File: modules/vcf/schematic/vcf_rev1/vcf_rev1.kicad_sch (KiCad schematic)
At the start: 0 parts

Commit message: Added project library Added 2N2978
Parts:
- added Q1: 2N2978, ProjectLib_Transient:TO-5-6, symbol ProjectLib_Transient:2N2978
- added Q2: BC548, Package_TO_SOT_THT:TO-92_Inline, symbol Transistor_BJT:BC548
- added R1, R2, R3, R4: 330, Resistor_THT:R_Axial_DIN0207_L6.3mm_D2.5mm_P10.16mm_Horizontal, symbol Device:R_US
- added RV1: 500, Potentiometer_THT:Potentiometer_Bourns_3296W_Vertical, symbol Device:R_Potentiometer_Trim_US
- added U1: OP275, Package_DIP:DIP-8_W7.62mm_Socket_LongPads, symbol Amplifier_Operational:OP275
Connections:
- new net: R3.2, RV1.1
- new net: Q1.5 (E2), R2.1
- new net: Q1.6 (B2), RV1.2
- new net: Q1.1 (E1), R1.1
- new net: Q2.1 (C), R1.2, R2.2
- new net: R4.1, RV1.3

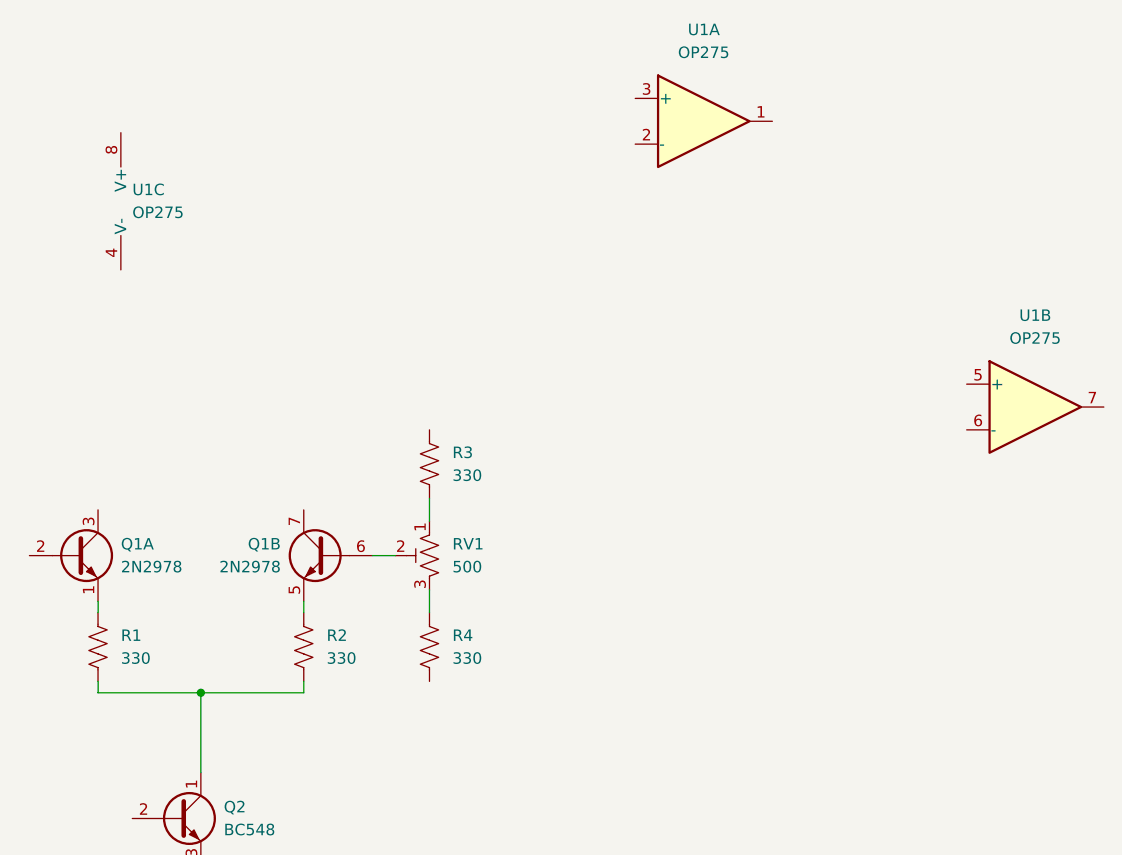
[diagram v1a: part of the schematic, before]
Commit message: added schematic for the headphones amplifier
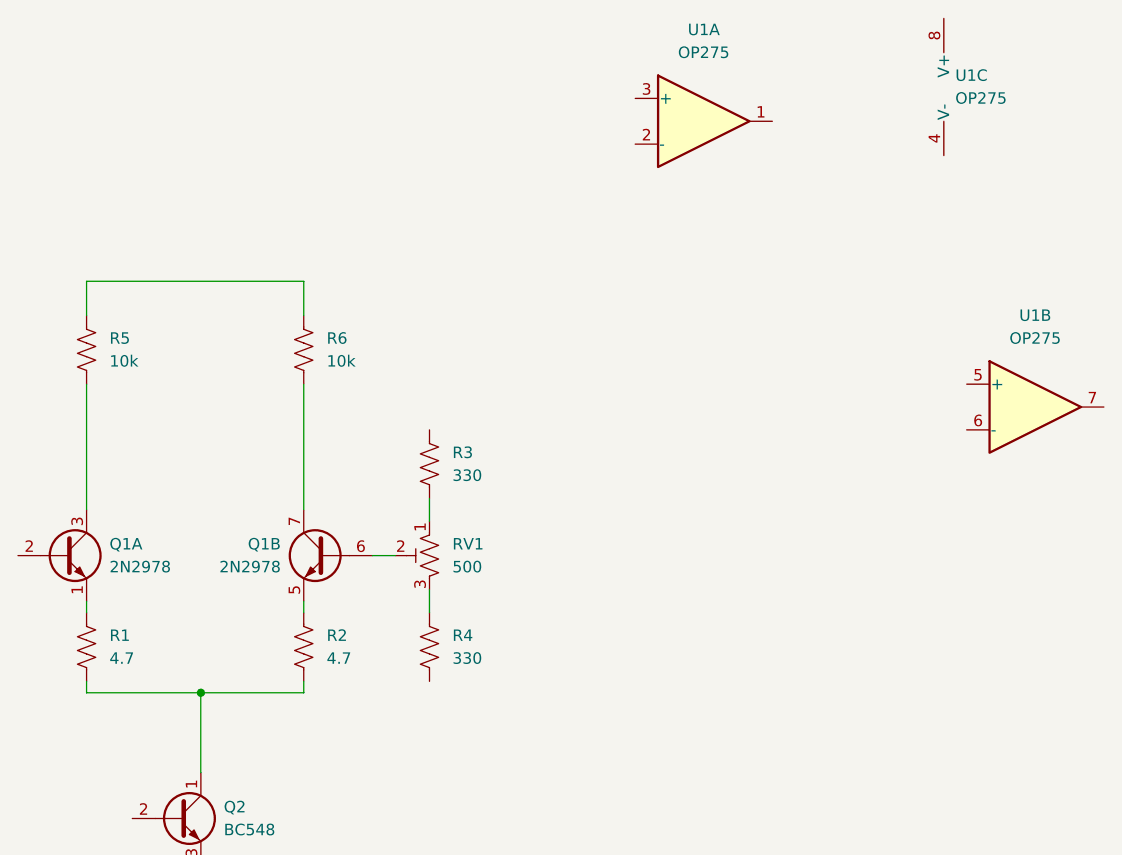
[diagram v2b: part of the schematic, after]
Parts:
- added R5, R6: 10k, Resistor_THT:R_Axial_DIN0207_L6.3mm_D2.5mm_P10.16mm_Horizontal, symbol Device:R_US
- added unit 1 of U1
- added unit 2 of U1
- R1, R2: value 330 -> 4.7
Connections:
- net at Q1.7 (C2): now also R6.2
- net at Q1.3 (C1): now also R5.2
- new net: R5.1, R6.1
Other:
- moved on the sheet: Q1A, R1, U1C
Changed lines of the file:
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@@
 	(wire
 		(pts
-			(xy 106.68 96.52) (xy 106.68 97.79)
+			(xy 129.54 60.96) (xy 129.54 64.77)
 		)
 		(stroke
@@
 	(wire
 		(pts
-			(xy 106.68 106.68) (xy 118.11 106.68)
+			(xy 105.41 96.52) (xy 105.41 97.79)
 		)
 		(stroke
@@
 	(wire
 		(pts
-			(xy 129.54 105.41) (xy 129.54 106.68)
+			(xy 105.41 106.68) (xy 118.11 106.68)
 		)
 		(stroke
@@
 	(wire
 		(pts
-			(xy 118.11 106.68) (xy 118.11 115.57)
+			(xy 129.54 72.39) (xy 129.54 86.36)
 		)
 		(stroke
@@
 	(wire
 		(pts
-			(xy 106.68 105.41) (xy 106.68 106.68)
+			(xy 105.41 72.39) (xy 105.41 86.36)
 		)
 		(stroke
@@
 		)
 	)
+	(wire
+		(pts
+			(xy 105.41 60.96) (xy 129.54 60.96)
+		)
+		(stroke
+			(width 0)
+			(type default)
+		)
+	)
+	(wire
+		(pts
+			(xy 105.41 64.77) (xy 105.41 60.96)
+		)
+		(stroke
+			(width 0)
+			(type default)
+		)
+	)
+	(wire
+		(pts
+			(xy 129.54 105.41) (xy 129.54 106.68)
+		)
+		(stroke
+			(width 0)
+			(type default)
+		)
+	)
+	(wire
+		(pts
+			(xy 118.11 106.68) (xy 118.11 115.57)
+		)
+		(stroke
+			(width 0)
+			(type default)
+		)
+	)
+	(wire
+		(pts
+			(xy 105.41 105.41) (xy 105.41 106.68)
+		)
+		(stroke
+			(width 0)
+			(type default)
+		)
+	)
+	(symbol
+		(lib_id "Device:R_US")
+		(at 105.41 68.58 0)
+		(unit 1)
+		(exclude_from_sim no)
+		(in_bom yes)
+		(on_board yes)
+		(dnp no)
+		(fields_autoplaced yes)
+		(property "Reference" "R5"
+			(at 107.95 67.3099 0)
+			(effects
+				(font
+					(size 1.27 1.27)
+				)
+				(justify left)
+			)
+		)
+		(property "Value" "10k"
+			(at 107.95 69.8499 0)
+			(effects
+				(font
+					(size 1.27 1.27)
+				)
+				(justify left)
+			)
+		)
+		(property "Footprint" "Resistor_THT:R_Axial_DIN0207_L6.3mm_D2.5mm_P10.16mm_Horizontal"
+			(at 106.426 68.834 90)
+			(effects
+				(font
+					(size 1.27 1.27)
+				)
+				(hide yes)
+			)
+		)
+		(property "Datasheet" "~"
+			(at 105.41 68.58 0)
+			(effects
+				(font
+					(size 1.27 1.27)
+				)
+				(hide yes)
+			)
+		)
+		(property "Description" "Resistor, US symbol"
+			(at 105.41 68.58 0)
+			(effects
+				(font
+					(size 1.27 1.27)
+				)
+				(hide yes)
+			)
+		)
+		(pin "2"
+		)
+		(pin "1"
+		)
+		(instances
+			(project "vcf_rev1"
+				(path "/3fbef366-554c-45da-b612-19de5a64a7d5"
+					(reference "R5")
+					(unit 1)
+				)
+			)
+		)
+	)
+	(symbol
+		(lib_id "Device:R_US")
+		(at 129.54 68.58 0)
+		(unit 1)
+		(exclude_from_sim no)
+		(in_bom yes)
+		(on_board yes)
+		(dnp no)
+		(fields_autoplaced yes)
+		(property "Reference" "R6"
+			(at 132.08 67.3099 0)
+			(effects
+				(font
+					(size 1.27 1.27)
+				)
+				(justify left)
+			)
+		)
+		(property "Value" "10k"
+			(at 132.08 69.8499 0)
+			(effects
+				(font
+					(size 1.27 1.27)
+				)
+				(justify left)
+			)
+		)
+		(property "Footprint" "Resistor_THT:R_Axial_DIN0207_L6.3mm_D2.5mm_P10.16mm_Horizontal"
+			(at 130.556 68.834 90)
+			(effects
+				(font
+					(size 1.27 1.27)
+				)
+				(hide yes)
+			)
+		)
+		(property "Datasheet" "~"
+			(at 129.54 68.58 0)
+			(effects
+				(font
+					(size 1.27 1.27)
+				)
+				(hide yes)
+			)
+		)
+		(property "Description" "Resistor, US symbol"
+			(at 129.54 68.58 0)
+			(effects
+				(font
+					(size 1.27 1.27)
+				)
+				(hide yes)
+			)
+		)
+		(pin "2"
+		)
+		(pin "1"
+		)
+		(instances
+			(project "vcf_rev1"
+				(path "/3fbef366-554c-45da-b612-19de5a64a7d5"
+					(reference "R6")
+					(unit 1)
+				)
+			)
+		)
+	)
 	(symbol
 		(lib_id "Amplifier_Operational:OP275")
-		(at 111.76 52.07 0)
+		(at 203.2 39.37 0)
 		(unit 3)
 		(exclude_from_sim no)
@@
 		(fields_autoplaced yes)
 		(property "Reference" "U1"
-			(at 110.49 50.7999 0)
+			(at 201.93 38.0999 0)
 			(effects
 				(font
@@
 		)
 		(property "Value" "OP275"
-			(at 110.49 53.3399 0)
+			(at 201.93 40.6399 0)
 			(effects
 				(font
@@
 		)
 		(property "Footprint" "Package_DIP:DIP-8_W7.62mm_Socket_LongPads"
-			(at 111.76 52.07 0)
+			(at 203.2 39.37 0)
 			(effects
 				(font
@@
 		)
 		(property "Datasheet" "https://www.analog.com/media/en/technical-documentation/data-sheets/OP275.pdf"
-			(at 111.76 52.07 0)
+			(at 203.2 39.37 0)
 			(effects
 				(font
@@
 		)
 		(property "Description" "Dual Bipolar/JFET, Audio Operational Amplifier, DIP-8/SOIC-8"
-			(at 111.76 52.07 0)
+			(at 203.2 39.37 0)
 			(effects
 				(font
@@
 	(symbol
 		(lib_id "Device:R_US")
-		(at 106.68 101.6 0)
+		(at 105.41 101.6 0)
 		(unit 1)
 		(exclude_from_sim no)
@@
 		(fields_autoplaced yes)
 		(property "Reference" "R1"
-			(at 109.22 100.3299 0)
-			(effects
-				(font
-					(size 1.27 1.27)
-				)
-				(justify left)
-			)
-		)
-		(property "Value" "330"
-			(at 109.22 102.8699 0)
+			(at 107.95 100.3299 0)
+			(effects
+				(font
+					(size 1.27 1.27)
+				)
+				(justify left)
+			)
+		)
+		(property "Value" "4.7"
+			(at 107.95 102.8699 0)
 			(effects
 				(font
@@
 		)
 		(property "Footprint" "Resistor_THT:R_Axial_DIN0207_L6.3mm_D2.5mm_P10.16mm_Horizontal"
-			(at 107.696 101.854 90)
+			(at 106.426 101.854 90)
 			(effects
 				(font
@@
 		)
 		(property "Datasheet" "~"
-			(at 106.68 101.6 0)
+			(at 105.41 101.6 0)
 			(effects
 				(font
@@
 		)
 		(property "Description" "Resistor, US symbol"
-			(at 106.68 101.6 0)
+			(at 105.41 101.6 0)
 			(effects
 				(font
@@
 	(symbol
 		(lib_id "ProjectLib_Transient:2N2978")
-		(at 104.14 91.44 0)
+		(at 102.87 91.44 0)
 		(unit 1)
 		(exclude_from_sim no)
@@
 		(fields_autoplaced yes)
 		(property "Reference" "Q1"
-			(at 109.22 90.1699 0)
+			(at 107.95 90.1699 0)
 			(effects
 				(font
@@
 		)
 		(property "Value" "2N2978"
-			(at 109.22 92.7099 0)
+			(at 107.95 92.7099 0)
 			(effects
 				(font
@@
 		)
 		(property "Footprint" "ProjectLib_Transient:TO-5-6"
-			(at 109.22 88.9 0)
+			(at 107.95 88.9 0)
 			(effects
 				(font
@@
 		)
 		(property "Datasheet" "~"
-			(at 104.14 91.44 0)
+			(at 102.87 91.44 0)
 			(effects
 				(font
@@
 		)
 		(property "Description" "Dual NPN transistor, 6 pin package"
-			(at 104.14 91.44 0)
+			(at 102.87 91.44 0)
 			(effects
 				(font
@@
 			)
 		)
-		(property "Value" "330"
+		(property "Value" "4.7"
 			(at 132.08 102.8699 0)
 			(effects

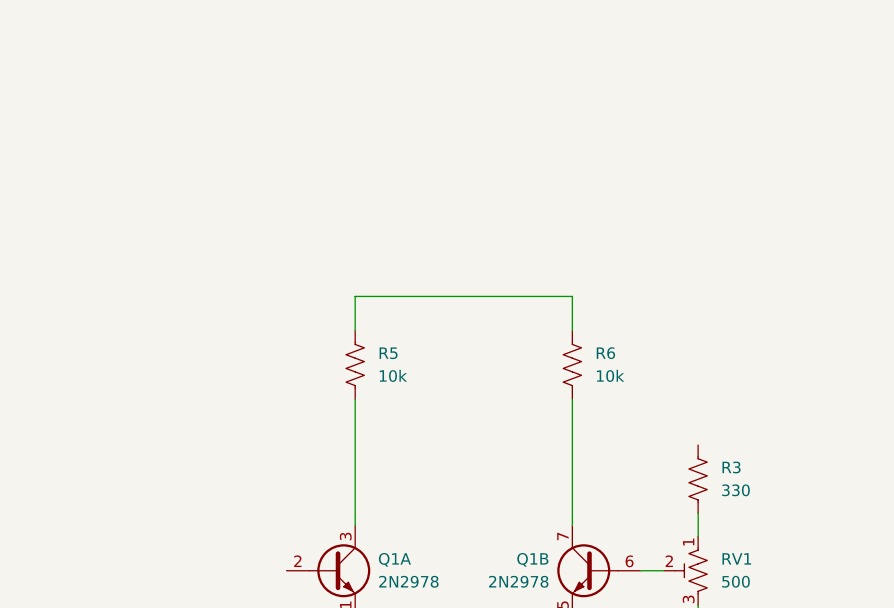
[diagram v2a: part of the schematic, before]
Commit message: added the noise generator module
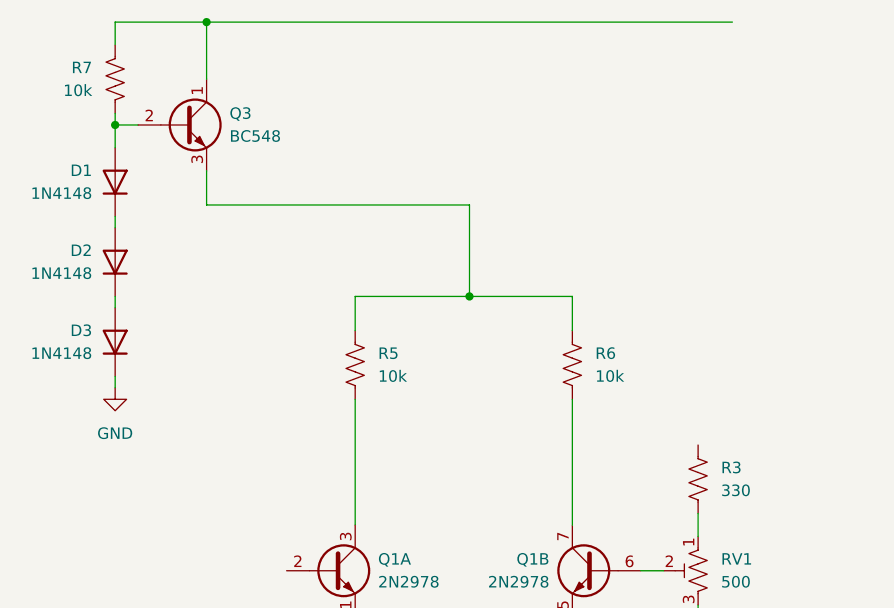
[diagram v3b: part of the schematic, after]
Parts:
- added D1, D2, D3: 1N4148, Diode_THT:D_DO-35_SOD27_P7.62mm_Horizontal, symbol Diode:1N4148
- added Q3: BC548, Package_TO_SOT_THT:TO-92_Inline, symbol Transistor_BJT:BC548
- added R7: 10k, Resistor_THT:R_Axial_DIN0207_L6.3mm_D2.5mm_P10.16mm_Horizontal, symbol Device:R_US
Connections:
- net at R5.1, R6.1: now also Q3.3 (E)
- new net: D2.1 (K), D3.2 (A)
- new net: D1.1 (K), D2.2 (A)
- new net: Q3.1 (C), R7.1
- new net: D1.2 (A), Q3.2 (B), R7.2
- new net GND: D3.1 (K)
